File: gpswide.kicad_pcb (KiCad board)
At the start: 2 copper layers, 36.8 x 27.9 mm, 12 parts, among them J1 GPS E406A, J2 Raspberry Pi, Q1 2N3904, U1 NE555

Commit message: cleaned up
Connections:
- net Net-(D1-Pad2) renamed RPI_PPS
- net Net-(J1-Pad1) renamed GPS_PPS
- net Net-(J1-Pad3) renamed GPS_TX
- net VCC renamed GPS_VCC
- C1 pad 2: GND -> GPX_GND
- C2 pad 2: GND -> GPX_GND
- D1 pad 1: GND -> GPX_GND
- J1 pad 6: GND -> GPS_GND
- J2 pad 6: GND -> GPX_GND
- Q1 pad 3: GND -> GPX_GND
- U1 pad 1: GND -> GPX_GND
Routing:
- net GND: track 66.8 -> 18.6 mm
- net GPX_GND: track 0.00 -> 46.9 mm

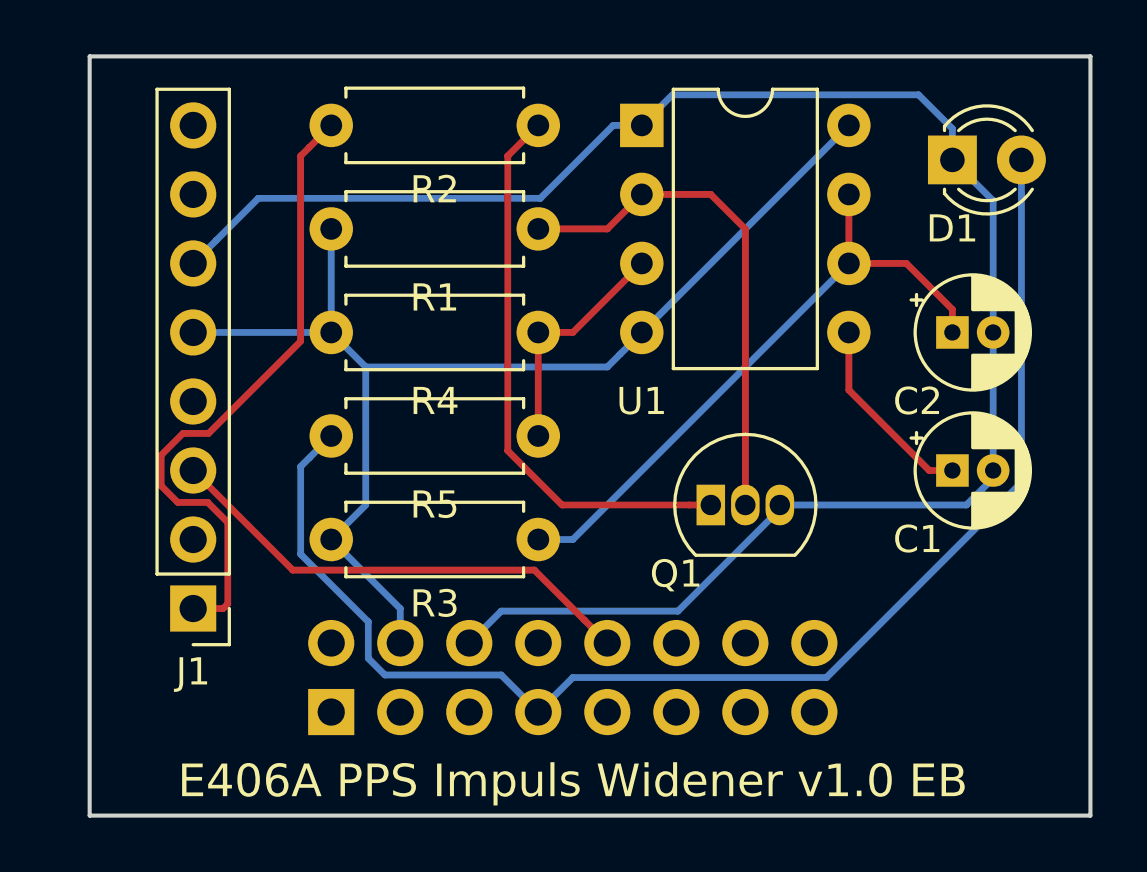
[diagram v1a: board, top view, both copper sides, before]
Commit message: ground plane added
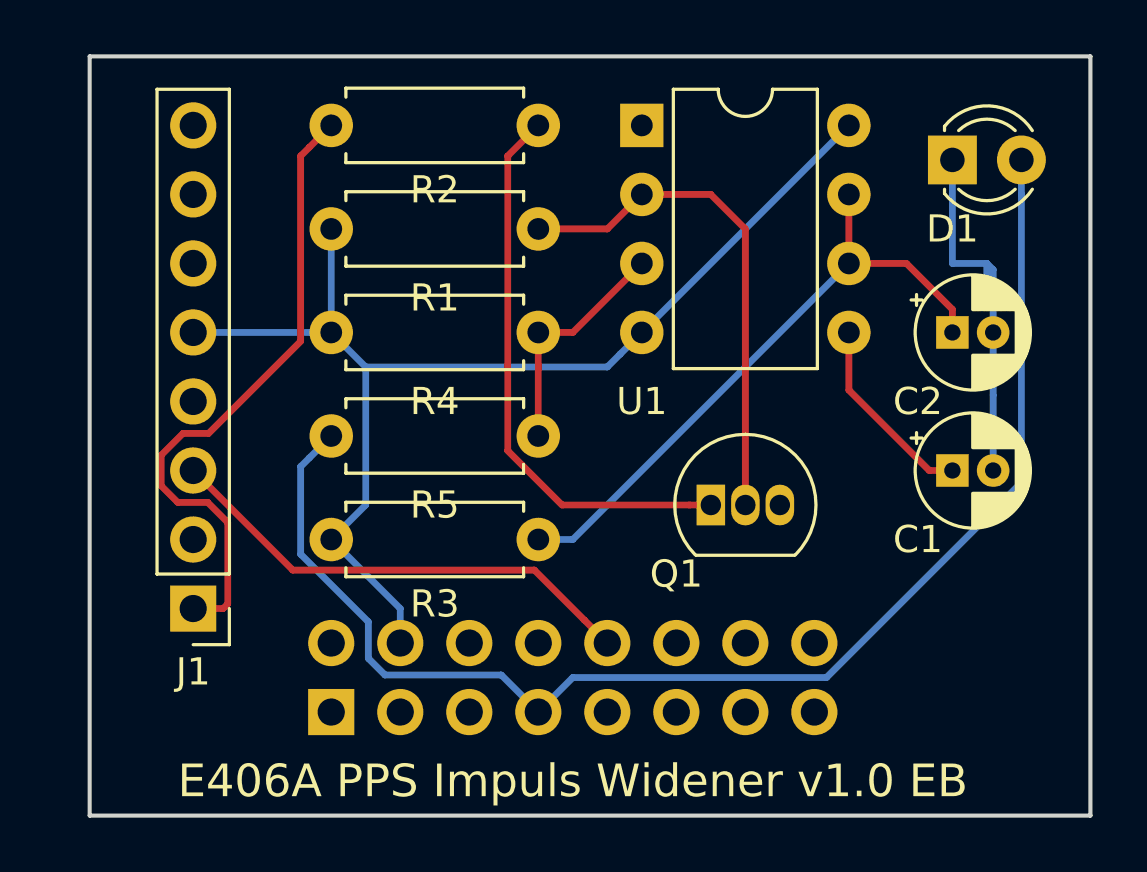
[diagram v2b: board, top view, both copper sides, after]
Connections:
- C1 pad 2: GPX_GND -> GND
- C2 pad 2: GPX_GND -> GND
- D1 pad 1: GPX_GND -> GND
- J1 pad 6: GPS_GND -> GND
- J2 pad 6: GPX_GND -> GND
- Q1 pad 3: GPX_GND -> GND
- U1 pad 1: GPX_GND -> GND
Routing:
- net GPX_GND: track 46.9 -> 0.00 mm
- net GND: track 18.6 -> 14.8 mm
- added copper zone on B.Cu, net GND

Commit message: v 1.1: Transistor footprint changed, resistor value changed
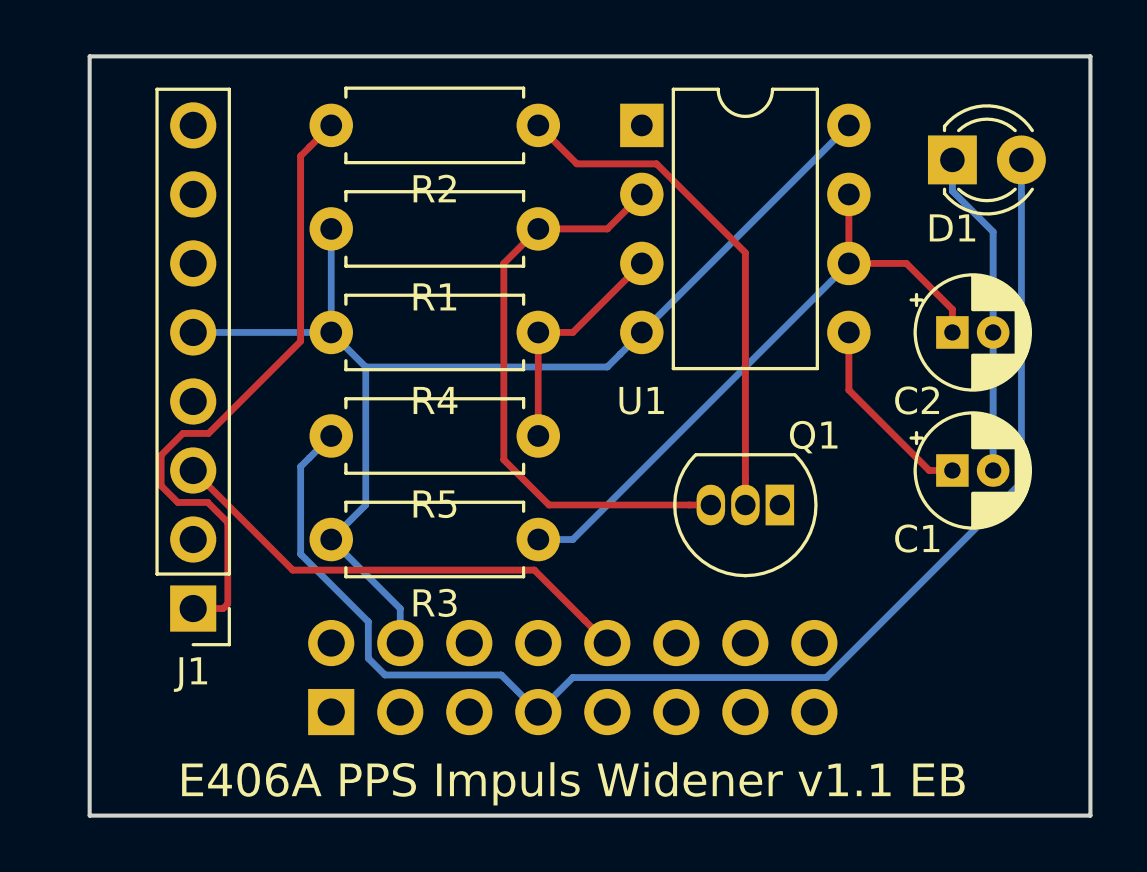
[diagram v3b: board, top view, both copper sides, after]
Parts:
- R2: value 100K -> 10K
- moved Q1 2.54 mm to (189.2, 40.6), turned to 180 degrees
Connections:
- Q1 pad 1: Net-(Q1-Pad1) -> GND
- Q1 pad 3: GND -> Net-(Q1-Pad3)
- R1 pad 2: Net-(Q1-Pad2) -> Net-(Q1-Pad3)
- R2 pad 1: Net-(Q1-Pad1) -> Net-(Q1-Pad2)
- U1 pad 2: Net-(Q1-Pad2) -> Net-(Q1-Pad3)
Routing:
- net Net-(Q1-Pad3): track 0.00 -> 21.7 mm
- net Net-(Q1-Pad1): track 20.7 -> 0.00 mm
- net GND: track 14.8 -> 12.8 mm
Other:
- board text added: "E406A PPS Impuls Widener v1.1 EB"
- board text removed: "E406A PPS Impuls Widener v1.0 EB"
